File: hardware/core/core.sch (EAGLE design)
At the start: 280 parts, among them IC1 MAX481CSA, IC10 MAX481CSA, IC11 MAX481CSA, IC12 MAX481CSA, IC13 MAX481CSA, IC14 MAX481CSA, IC15 MAX481CSA, IC16 MAX481CSA, IC17 MAX481CSA, IC18 MAX481CSA, IC19 MAX481CSA, IC2 LD117AS12TR, IC20 MAX481CSA, IC21 MAX481CSA, IC3 MAX481CSA, IC4 MAX481CSA, IC5 MAX481CSA, IC6 MAX481CSA, IC7 MAX481CSA, IC8 MAX481CSA, IC9 MAX481CSA

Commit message: Nova 3.0 in progress. Needs line drivers.
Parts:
- added C35, C36: 10uf, rcl:C-USC0603
- added C6: 1uf, rcl:C-USC0805
- added D81, D86, D91: red, SparkFun-LED:LED0603
- added D82, D87, D92: green, SparkFun-LED:LED0603
- added D83, D88, D93: blue, SparkFun-LED:LED0603
- added D84, D89: white, SparkFun-LED:LED0603
- added D85, D90, D94: yellow, SparkFun-LED:LED0603
- added IC22: LD117AS12TR, v-reg:LD117AS12TR
- added R1, R107, R108, R109, R110, R111, R112, R113, R114, R115, R116, R117, R118, R119, R120, R121, R122, R123, R124, R2: 120, rcl:R-US_R0603
- added R125, R126, R127, R128, R129, R130, R139: 1k, rcl:R-US_R0603
- added R131: 2.2k, rcl:R-US_R0603
- added R132: 12k, rcl:R-US_R0603
- added R133, R134, R135, R136, R137: 10k, rcl:R-US_R0603
- added R138: 10, rcl:R-US_R1206
- added S1, S2, S3, S4, S5: MOMENTARY-SWITCH-SPST-PTH-6.0MM, SparkFun-Switches:MOMENTARY-SWITCH-SPST-PTH-6.0MM
- added ULN2: (no value), SparkFun-IC-Special-Function:ULN2803SOICW
- R68: value 68 -> 10; device rcl:R-US_R0603 -> rcl:R-US_R1206; LCSC_PART C25804 -> C17903
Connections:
- new net N$151: D84.A, R129.2
- new net N$152: D85.A, R128.2
- new net N$153: D83.A, R127.2
- new net N$154: D82.A, R126.2
- new net N$155: D81.A, R125.2
- new net N$156: D91.C, R130.1
- new net N$157: D92.C, R131.1
- new net N$158: D93.C, R132.1
- new net N$159: D94.C, R139.1
- net +12V: now also D93.A, ULN2.10
- net +3V3: now also C36.1, D86.A, D87.A, D88.A, D89.A, D90.A, D91.A, IC22.OUT, R133.1, R134.1, R135.1, R136.1, R137.1, R138.2
- net +5V: now also C35.1, C6.1, D92.A, IC22.IN, R125.1, R126.1, R127.1, R128.1, R129.1
- net 13: now also D94.A
- net 23: now also ULN2.8
- net 25: now also ULN2.7
- net 26: now also ULN2.6
- net 27: now also ULN2.5
- net 32: now also ULN2.4
- net GND: now also C35.2, C36.2, C6.2, IC22.ADJ, R130.2, R131.2, R132.2, R139.2, S1.2, S2.2, S3.2, S4.2, S5.2, ULN2.9
- net H10: now also D88.C, R135.2, S3.1
- net H11: now also D90.C, R134.2, S4.1
- net H12: now also D89.C, R133.2, S5.1
- net H13: now also ULN2.3
- net H14: now also ULN2.2
- net H15: now also ULN2.1
- net H8: now also D86.C, R137.2, S1.1
- net H9: now also D87.C, R136.2, S2.1
- net N$108: now also R1.2
- net N$109: now also R1.1
- net N$110: now also R2.2
- net N$111: now also R2.1
- net N$112: now also R107.2
- net N$113: now also R107.1
- net N$114: now also R108.2
- net N$115: now also R108.1
- net N$116: now also R109.2
- net N$117: now also R109.1
- net N$118: now also R110.2
- net N$119: now also R110.1
- net N$120: now also R111.2
- net N$121: now also R111.1
- net N$122: now also R112.2
- net N$123: now also R112.1
- net N$124: now also R113.2
- net N$125: now also R113.1
- net N$126: now also R114.2
- net N$127: now also R114.1
- net N$128: now also R115.2
- net N$129: now also R115.1
- net N$130: now also R116.2
- net N$131: now also R116.1
- net N$132: now also R117.2
- net N$133: now also R117.1
- net N$134: now also R118.2
- net N$135: now also R118.1
- net N$136: now also R119.2
- net N$137: now also R119.1
- net N$138: now also R120.2
- net N$139: now also R120.1
- net N$140: now also R121.2
- net N$141: now also R121.1
- net N$142: now also R122.2
- net N$143: now also R122.1
- net N$144: now also R123.2
- net N$145: now also R123.1
- net N$146: now also R124.2
- net N$147: now also R124.1
- net N$148: now also ULN2.16
- net N$149: now also ULN2.17
- net N$150: now also ULN2.18
- net N$51: now also D81.C, ULN2.11
- net N$56: now also D82.C, ULN2.12
- net N$57: now also D83.C, ULN2.13
- net N$58: now also D85.C, ULN2.14
- net N$59: now also D84.C, ULN2.15
- net N$89: now also R138.1
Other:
- note added: "TODO: Power light Safety Engaged Light"
- moved on the sheet: ACCESSORY, ACCESSORY_GPIO, ULN1

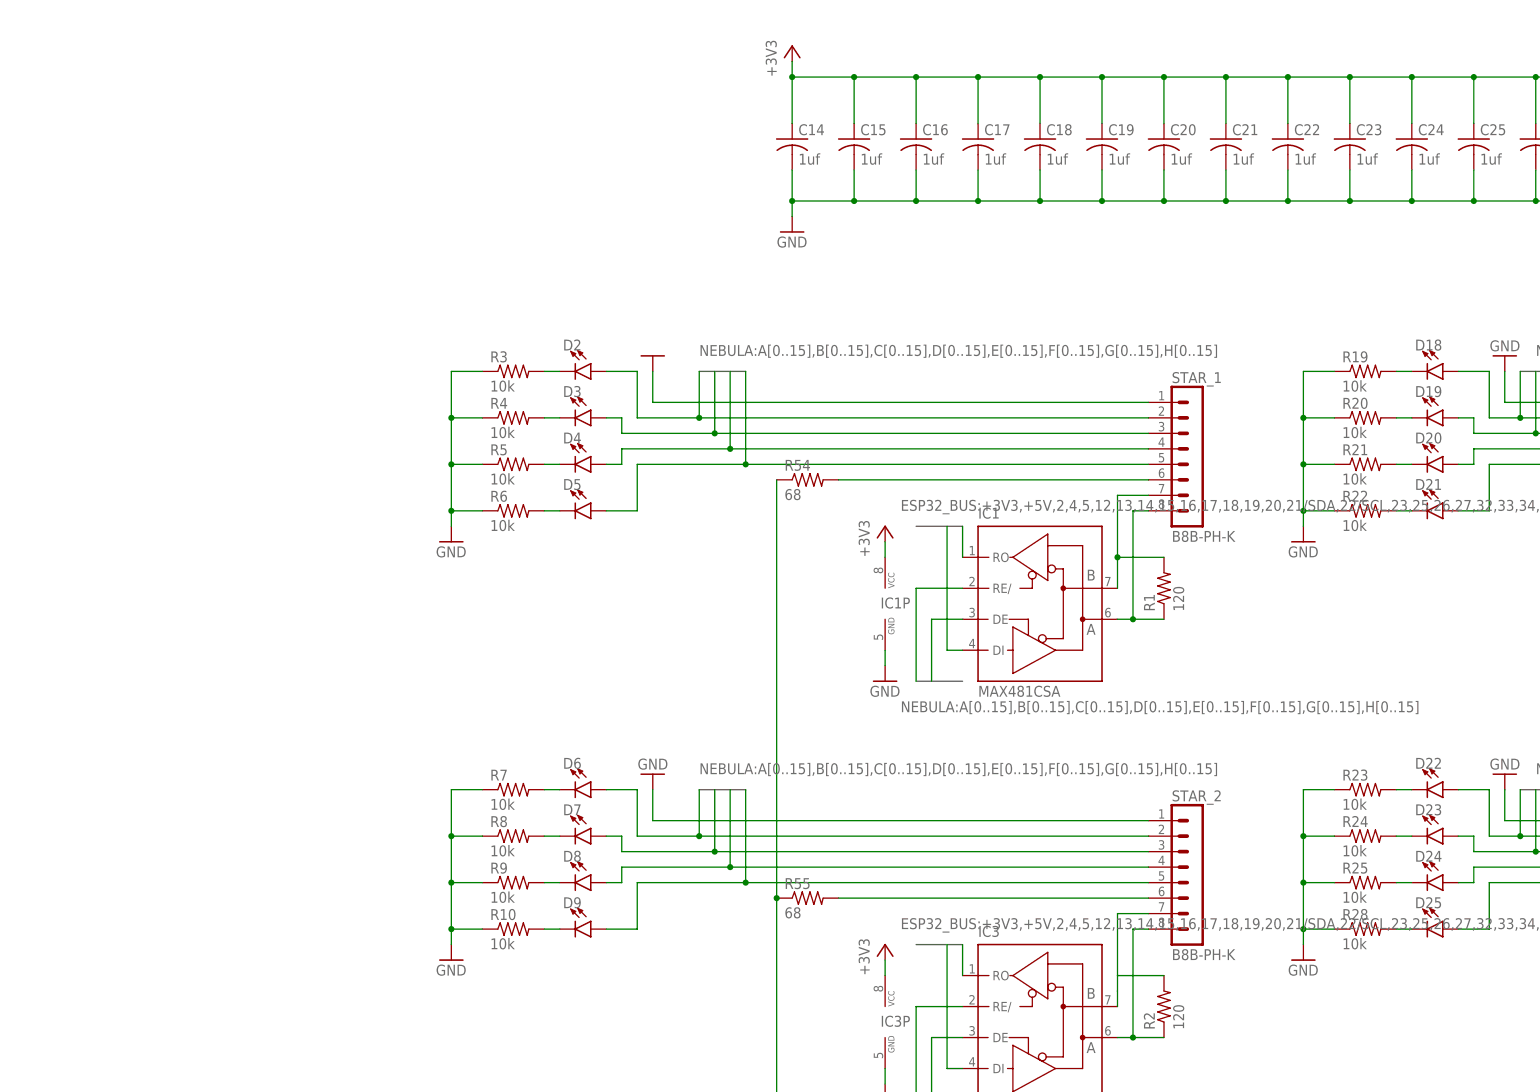
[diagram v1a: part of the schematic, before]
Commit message: start of adding ULN to the outputs
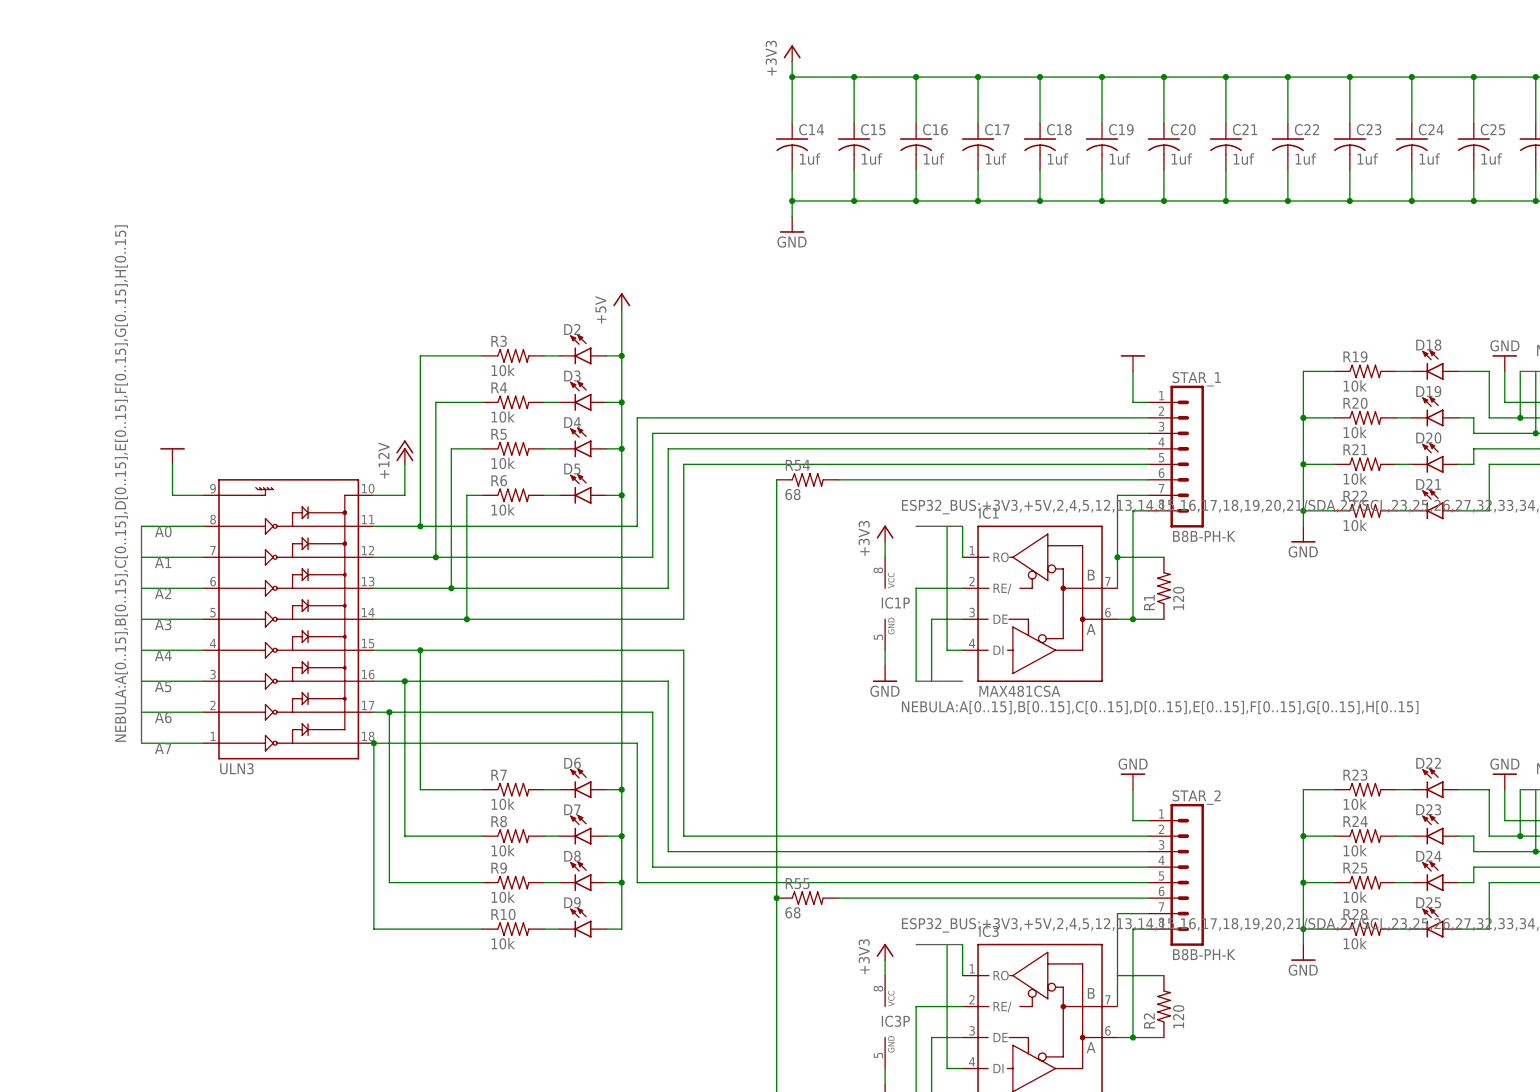
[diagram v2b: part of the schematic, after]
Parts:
- added ULN3: (no value), SparkFun-IC-Special-Function:ULN2803SOICW
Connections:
- new net N$160: R3.1, STAR_1.2, ULN3.11
- new net N$161: R4.1, STAR_1.3, ULN3.12
- new net N$162: R5.1, STAR_1.4, ULN3.13
- new net N$163: R6.1, STAR_1.5, ULN3.14
- new net N$164: R10.1, STAR_2.5, ULN3.18
- new net N$165: R9.1, STAR_2.4, ULN3.17
- new net N$166: R8.1, STAR_2.3, ULN3.16
- new net N$167: R7.1, STAR_2.2, ULN3.15
- net +12V: now also ULN3.10
- net +5V: now also D2.A, D3.A, D4.A, D5.A, D6.A, D7.A, D8.A, D9.A
- net A0: now also ULN3.8; no longer D2.A, STAR_1.2
- net A1: now also ULN3.7; no longer D3.A, STAR_1.3
- net A2: now also ULN3.6; no longer D4.A, STAR_1.4
- net A3: now also ULN3.5; no longer D5.A, STAR_1.5
- net A4: now also ULN3.4; no longer D6.A, STAR_2.2
- net A5: now also ULN3.3; no longer D7.A, STAR_2.3
- net A6: now also ULN3.2; no longer D8.A, STAR_2.4
- net A7: now also ULN3.1; no longer D9.A, STAR_2.5
- net GND: now also ULN3.9; no longer R10.1, R3.1, R4.1, R5.1, R6.1, R7.1, R8.1, R9.1
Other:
- moved on the sheet: D2, D3, D4, D5, R3, R4, R5, R6

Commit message: More Progress
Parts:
- added C37, C38, C39, C40, C41, C42, C43, C44, C45, C46, C47, C48, C49, C50, C51, C52, C53, C54, C55, C56, C57, C58, C59, C60, C61, C62, C63, C64, C65, C66, C67, C68, C73, C74, C75, C76, C77, C78, C79, C80, C81, C82, C83, C84, C85, C86, C87, C88: 1nf, rcl:C-USC0603
- added C69, C70, C71, C72, C89: 2200uf, rcl:CPOL-USE5-13
- added C90: 1uf, rcl:C-USC0805
- added C91, C92: 10uf, rcl:C-USC0603
- added IC23: LD117AS12TR, v-reg:LD117AS12TR
- added R140, R141, R142, R143, R144, R145, R146, R147, R148, R149, R150, R151, R152, R153, R154, R155, R156, R157, R158, R159, R160, R161, R162, R163, R164, R165, R166, R167, R168, R169, R170, R171, R172, R173, R174, R175, R176, R177, R178, R179, R180, R181, R182, R183, R184, R185, R186, R187, R188, R189, R190, R191, R192, R193, R194, R195, R196, R197, R198, R199, R200, R201, R202, R203, R204, R205, R206, R207, R208, R209, R210, R211, R212, R213, R214, R215, R216, R217, R218, R219: 68, rcl:R-US_R0603
- added ULN10, ULN11, ULN12, ULN4, ULN5, ULN6, ULN7, ULN8, ULN9: (no value), SparkFun-IC-Special-Function:ULN2803SOICW
- LEDARRAY: device SparkFun-Connectors:CONN_03 -> SparkFun-Connectors:CONN_03LONGPADS
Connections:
- new net N$168: R143.2, STAR_1.2
- new net N$169: R142.2, STAR_1.3
- new net N$170: R141.2, STAR_1.4
- new net N$171: R140.2, STAR_1.5
- new net N$172: R147.2, STAR_2.2
- new net N$173: R146.2, STAR_2.3
- new net N$174: R145.2, STAR_2.4
- new net N$175: R144.2, STAR_2.5
- new net N$176: R151.2, STAR_3.2
- new net N$177: R150.2, STAR_3.3
- new net N$178: R149.2, STAR_3.4
- new net N$179: R148.2, STAR_3.5
- new net N$180: R155.2, STAR_4.2
- new net N$181: R154.2, STAR_4.3
- new net N$182: R153.2, STAR_4.4
- new net N$183: R152.2, STAR_4.5
- new net N$184: C45.1, R11.1, R151.1, ULN4.11
- new net N$185: C46.1, R12.1, R150.1, ULN4.12
- new net N$186: C47.1, R13.1, R149.1, ULN4.13
- new net N$187: C48.1, R14.1, R148.1, ULN4.14
- new net N$188: C52.1, R152.1, R18.1, ULN4.18
- new net N$189: C51.1, R153.1, R17.1, ULN4.17
- new net N$190: C50.1, R154.1, R16.1, ULN4.16
- new net N$191: C49.1, R15.1, R155.1, ULN4.15
- new net N$192: C53.1, R159.1, R19.1, ULN5.11
- new net N$193: C56.1, R156.1, R22.1, ULN5.14
- new net N$194: C55.1, R157.1, R21.1, ULN5.13
- new net N$195: C54.1, R158.1, R20.1, ULN5.12
- new net N$196: C60.1, R160.1, R28.1, ULN5.18
- new net N$197: C59.1, R161.1, R25.1, ULN5.17
- new net N$198: C58.1, R162.1, R24.1, ULN5.16
- new net N$199: C57.1, R163.1, R23.1, ULN5.15
- new net N$200: R159.2, STAR_5.2
- new net N$201: R158.2, STAR_5.3
- new net N$202: R157.2, STAR_5.4
- new net N$203: R156.2, STAR_5.5
- new net N$204: R163.2, STAR_6.2
- new net N$205: R162.2, STAR_6.3
- new net N$206: R161.2, STAR_6.4
- new net N$207: R160.2, STAR_6.5
- new net N$208: R167.2, STAR_7.2
- new net N$209: R166.2, STAR_7.3
- new net N$210: R165.2, STAR_7.4
- new net N$211: R164.2, STAR_7.5
- new net N$212: R171.2, STAR_8.2
- new net N$213: R170.2, STAR_8.3
- new net N$214: R169.2, STAR_8.4
- new net N$215: R168.2, STAR_8.5
- new net N$216: C61.1, R167.1, R29.1, ULN6.11
- new net N$217: C62.1, R166.1, R30.1, ULN6.12
- new net N$218: C63.1, R165.1, R31.1, ULN6.13
- new net N$219: C64.1, R164.1, R32.1, ULN6.14
- new net N$220: C68.1, R168.1, R36.1, ULN6.18
- new net N$221: C67.1, R169.1, R35.1, ULN6.17
- new net N$222: C66.1, R170.1, R34.1, ULN6.16
- new net N$223: C65.1, R171.1, R33.1, ULN6.15
- new net N$224: R175.2, STAR_9.2
- new net N$225: R179.2, STAR_10.2
- new net N$226: R178.2, STAR_10.3
- new net N$227: R174.2, STAR_9.3
- new net N$228: R173.2, STAR_9.4
- new net N$229: R172.2, STAR_9.5
- new net N$230: R177.2, STAR_10.4
- new net N$231: R176.2, STAR_10.5
- new net N$232: R183.2, STAR_11.2
- new net N$233: R182.2, STAR_11.3
- new net N$234: R181.2, STAR_11.4
- new net N$235: R180.2, STAR_11.5
- new net N$236: R187.2, STAR_12.2
- new net N$237: R186.2, STAR_12.3
- new net N$238: R185.2, STAR_12.4
- new net N$239: R184.2, STAR_12.5
- new net N$240: C73.1, R175.1, R37.1, ULN7.11
- new net N$241: C74.1, R174.1, R38.1, ULN7.12
- new net N$242: C75.1, R173.1, R39.1, ULN7.13
- new net N$243: C76.1, R172.1, R40.1, ULN7.14
- new net N$244: R191.2, STAR_13.2
- new net N$245: C79.1, R177.1, R43.1, ULN7.17
- new net N$246: C78.1, R178.1, R42.1, ULN7.16
- new net N$247: C77.1, R179.1, R41.1, ULN7.15
- new net N$248: C81.1, R183.1, R45.1, ULN8.11
- new net N$249: C82.1, R182.1, R46.1, ULN8.12
- new net N$250: C83.1, R181.1, R47.1, ULN8.13
- new net N$251: C84.1, R180.1, R48.1, ULN8.14
- new net N$252: C80.1, R176.1, R44.1, ULN7.18
- new net N$253: C87.1, R185.1, R51.1, ULN8.17
- new net N$254: C86.1, R186.1, R50.1, ULN8.16
- new net N$255: C85.1, R187.1, R49.1, ULN8.15
- new net N$256: R190.2, STAR_13.3
- new net N$257: R189.2, STAR_13.4
- new net N$258: R188.2, STAR_13.5
- new net N$259: R196.2, STAR_14.2
- new net N$260: C88.1, R184.1, R52.1, ULN8.18
- new net N$261: R195.2, STAR_14.3
- new net N$262: R194.2, STAR_14.4
- new net N$263: R193.2, STAR_14.5
- new net N$264: R199.2, STAR_15.2
- new net N$265: R198.2, STAR_15.3
- new net N$266: R192.2, STAR_15.5
- new net N$267: R197.2, STAR_15.4
- new net N$268: R203.2, STAR_16.2
- new net N$269: R202.2, STAR_16.3
- new net N$270: R201.2, STAR_16.4
- new net N$271: R200.2, STAR_16.5
- new net N$272: R216.2, STAR_20.5
- new net N$273: R217.2, STAR_20.4
- new net N$274: R218.2, STAR_20.3
- new net N$275: R219.2, STAR_20.2
- new net N$276: R212.2, STAR_19.5
- new net N$277: R213.2, STAR_19.4
- new net N$278: R214.2, STAR_19.3
- new net N$279: R215.2, STAR_19.2
- new net N$280: R208.2, STAR_18.5
- new net N$281: R209.2, STAR_18.4
- new net N$282: R210.2, STAR_18.3
- new net N$283: R211.2, STAR_18.2
- new net N$284: R204.2, STAR_17.5
- new net N$285: R205.2, STAR_17.4
- new net N$286: R206.2, STAR_17.3
- new net N$287: R207.2, STAR_17.2
- net +12V: now also C89.+, C90.1, C92.1, IC23.IN, ULN4.10, ULN5.10, ULN6.10, ULN7.10, ULN8.10
- net +3V3: now also C70.+, C72.+
- net +5V: now also C69.+, C71.+, C91.1, D10.A, D11.A, D12.A, D13.A, D14.A, D15.A, D16.A, D17.A, D18.A, D19.A, D20.A, D21.A, D22.A, D23.A, D24.A, D25.A, D26.A, D27.A, D28.A, D29.A, D30.A, D31.A, D32.A, D33.A, D34.A, D35.A, D36.A, D37.A, D38.A, D39.A, D40.A, D41.A, D42.A, D43.A, D44.A, D45.A, D46.A, D47.A, D48.A, D49.A, IC23.OUT
- net A10: now also ULN4.6; no longer D12.A, STAR_3.4
- net A11: now also ULN4.5; no longer D13.A, STAR_3.5
- net A12: now also ULN4.4; no longer D14.A, STAR_4.2
- net A13: now also ULN4.3; no longer D15.A, STAR_4.3
- net A14: now also ULN4.2; no longer D16.A, STAR_4.4
- net A15: now also ULN4.1; no longer D17.A, STAR_4.5
- net A8: now also ULN4.8; no longer D10.A, STAR_3.2
- net A9: now also ULN4.7; no longer D11.A, STAR_3.3
- net B0: now also ULN5.8; no longer D18.A, STAR_5.2
- net B1: now also ULN5.7; no longer D19.A, STAR_5.3
- net B10: now also ULN6.6; no longer D28.A, STAR_7.4
- net B11: now also ULN6.5; no longer D29.A, STAR_7.5
- net B12: now also ULN6.4; no longer D30.A, STAR_8.2
- net B13: now also ULN6.3; no longer D31.A, STAR_8.3
- net B14: now also ULN6.2; no longer D32.A, STAR_8.4
- net B15: now also ULN6.1; no longer D33.A, STAR_8.5
- net B2: now also ULN5.6; no longer D20.A, STAR_5.4
- net B3: now also ULN5.5; no longer D21.A, STAR_5.5
- net B4: now also ULN5.4; no longer D22.A, STAR_6.2
- net B5: now also ULN5.3; no longer D23.A, STAR_6.3
- net B6: now also ULN5.2; no longer D24.A, STAR_6.4
- net B7: now also ULN5.1; no longer D25.A, STAR_6.5
- net B8: now also ULN6.8; no longer D26.A, STAR_7.2
- net B9: now also ULN6.7; no longer D27.A, STAR_7.3
- net C0: now also ULN7.8; no longer D34.A, STAR_9.2
- net C1: now also ULN7.7; no longer D35.A, STAR_9.3
- net C10: now also ULN8.6; no longer D44.A, STAR_11.4
- net C11: now also ULN8.5; no longer D45.A, STAR_11.5
- net C12: now also ULN8.4; no longer D46.A, STAR_12.2
- net C13: now also ULN8.3; no longer D47.A, STAR_12.3
- net C14: now also ULN8.2; no longer D48.A, STAR_12.4
- net C15: now also ULN8.1; no longer D49.A, STAR_12.5
- net C2: now also ULN7.6; no longer D36.A, STAR_9.4
- net C3: now also ULN7.5; no longer D37.A, STAR_9.5
- net C4: now also ULN7.4; no longer D38.A, STAR_10.2
- net C5: now also ULN7.3; no longer D39.A, STAR_10.3
- net C6: now also ULN7.2; no longer D40.A, STAR_10.4
- net C7: now also ULN7.1; no longer D41.A, STAR_10.5
- net C8: now also ULN8.8; no longer D42.A, STAR_11.2
- net C9: now also ULN8.7; no longer D43.A, STAR_11.3
- net D0: no longer D1.A, STAR_13.2
- net D1: no longer D50.A, STAR_13.3
- net D10: no longer D59.A, STAR_15.4
- net D11: no longer D60.A, STAR_15.5
- net D12: no longer D61.A, STAR_16.2
- net D13: no longer D62.A, STAR_16.3
- net D14: no longer D63.A, STAR_16.4
- net D15: no longer D64.A, STAR_16.5
- net D2: no longer D51.A, STAR_13.4
- net D3: no longer D52.A, STAR_13.5
- net D4: no longer D53.A, STAR_14.2
- net D5: no longer D54.A, STAR_14.3
- net D6: no longer D55.A, STAR_14.4
- net D7: no longer D56.A, STAR_14.5
- net D8: no longer D57.A, STAR_15.2
- net D9: no longer D58.A, STAR_15.3
- net E0: no longer D65.A, STAR_17.2
- net E1: no longer D66.A, STAR_17.3
- net E10: no longer D75.A, STAR_19.4
- net E11: no longer D76.A, STAR_19.5
- net E12: no longer D77.A, STAR_20.2
- net E13: no longer D78.A, STAR_20.3
- net E14: no longer D79.A, STAR_20.4
- net E15: no longer D80.A, STAR_20.5
- net E2: no longer D67.A, STAR_17.4
- net E3: no longer D68.A, STAR_17.5
- net E4: no longer D69.A, STAR_18.2
- net E5: no longer D70.A, STAR_18.3
- net E6: no longer D71.A, STAR_18.4
- net E7: no longer D72.A, STAR_18.5
- net E8: no longer D73.A, STAR_19.2
- net E9: no longer D74.A, STAR_19.3
- net GND: now also C37.2, C38.2, C39.2, C40.2, C41.2, C42.2, C43.2, C44.2, C45.2, C46.2, C47.2, C48.2, C49.2, C50.2, C51.2, C52.2, C53.2, C54.2, C55.2, C56.2, C57.2, C58.2, C59.2, C60.2, C61.2, C62.2, C63.2, C64.2, C65.2, C66.2, C67.2, C68.2, C69.-, C70.-, C71.-, C72.-, C73.2, C74.2, C75.2, C76.2, C77.2, C78.2, C79.2, C80.2, C81.2, C82.2, C83.2, C84.2, C85.2, C86.2, C87.2, C88.2, C89.-, C90.2, C91.2, C92.2, IC23.ADJ, ULN4.9, ULN5.9, ULN6.9, ULN7.9, ULN8.9; no longer R11.1, R12.1, R13.1, R14.1, R15.1, R16.1, R17.1, R18.1, R19.1, R20.1, R21.1, R22.1, R23.1, R24.1, R25.1, R28.1, R29.1, R30.1, R31.1, R32.1, R33.1, R34.1, R35.1, R36.1, R37.1, R38.1, R39.1, R40.1, R41.1, R42.1, R43.1, R44.1, R45.1, R46.1, R47.1, R48.1, R49.1, R50.1, R51.1, R52.1
- net N$160: now also C37.1, R143.1; no longer STAR_1.2
- net N$161: now also C38.1, R142.1; no longer STAR_1.3
- net N$162: now also C39.1, R141.1; no longer STAR_1.4
- net N$163: now also C40.1, R140.1; no longer STAR_1.5
- net N$164: now also C44.1, R144.1; no longer STAR_2.5
- net N$165: now also C43.1, R145.1; no longer STAR_2.4
- net N$166: now also C42.1, R146.1; no longer STAR_2.3
- net N$167: now also C41.1, R147.1; no longer STAR_2.2
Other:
- moved on the sheet: C10, C11, C12, C13, C14, C15, C16, C17, C18, C19, C20, C21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

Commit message: Schematic Capture is complete
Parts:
- added C100, C101, C102, C103, C104, C105, C106, C107, C108, C109, C110, C111, C112, C113, C114, C115, C116, C117, C118, C119, C120, C121, C122, C123, C124, C93, C94, C95, C96, C97, C98, C99: 1nf, rcl:C-USC0603
- added JP2, JP3: (no value), pinhead:PINHD-1X4
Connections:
- new net N$288: C97.1, R199.1, R75.1, ULN10.11
- new net N$289: C98.1, R198.1, R76.1, ULN10.12
- new net N$290: C99.1, R197.1, R77.1, ULN10.13
- new net N$291: C100.1, R192.1, R78.1, ULN10.14
- new net N$292: C108.1, R200.1, R82.1, ULN10.18
- new net N$293: C107.1, R201.1, R81.1, ULN10.17
- new net N$294: C106.1, R202.1, R80.1, ULN10.16
- new net N$295: C105.1, R203.1, R79.1, ULN10.15
- new net N$296: C93.1, R191.1, R53.1, ULN9.11
- new net N$297: C94.1, R190.1, R66.1, ULN9.12
- new net N$298: C95.1, R189.1, R69.1, ULN9.13
- new net N$299: C96.1, R188.1, R70.1, ULN9.14
- new net N$300: C104.1, R193.1, R74.1, ULN9.18
- new net N$301: C103.1, R194.1, R73.1, ULN9.17
- new net N$302: C102.1, R195.1, R72.1, ULN9.16
- new net N$303: C101.1, R196.1, R71.1, ULN9.15
- new net N$304: C109.1, R207.1, R87.1, ULN11.11
- new net N$305: C110.1, R206.1, R88.1, ULN11.12
- new net N$306: C111.1, R205.1, R89.1, ULN11.13
- new net N$307: C112.1, R204.1, R90.1, ULN11.14
- new net N$308: C116.1, R208.1, R94.1, ULN11.18
- new net N$309: C115.1, R209.1, R93.1, ULN11.17
- new net N$310: C114.1, R210.1, R92.1, ULN11.16
- new net N$311: C113.1, R211.1, R91.1, ULN11.15
- new net N$312: C117.1, R215.1, R95.1, ULN12.11
- new net N$313: C118.1, R214.1, R96.1, ULN12.12
- new net N$314: C119.1, R213.1, R97.1, ULN12.13
- new net N$315: C120.1, R212.1, R98.1, ULN12.14
- new net N$316: C124.1, R102.1, R216.1, ULN12.18
- new net N$317: C123.1, R101.1, R217.1, ULN12.17
- new net N$318: C122.1, R100.1, R218.1, ULN12.16
- new net N$319: C121.1, R219.1, R99.1, ULN12.15
- net +12V: now also ULN10.10, ULN11.10, ULN12.10, ULN9.10
- net +3V3: now also JP2.4, JP3.1
- net +5V: now also D1.A, D50.A, D51.A, D52.A, D53.A, D54.A, D55.A, D56.A, D57.A, D58.A, D59.A, D60.A, D61.A, D62.A, D63.A, D64.A, D65.A, D66.A, D67.A, D68.A, D69.A, D70.A, D71.A, D72.A, D73.A, D74.A, D75.A, D76.A, D77.A, D78.A, D79.A, D80.A
- net 2: now also JP2.2
- net 21/SDA: now also JP3.4
- net 22/SCL: now also JP3.3
- net 5: now also JP2.3
- net D0: now also ULN9.8
- net D1: now also ULN9.7
- net D10: now also ULN10.6
- net D11: now also ULN10.5
- net D12: now also ULN10.4
- net D13: now also ULN10.3
- net D14: now also ULN10.2
- net D15: now also ULN10.1
- net D2: now also ULN9.6
- net D3: now also ULN9.5
- net D4: now also ULN9.4
- net D5: now also ULN9.3
- net D6: now also ULN9.2
- net D7: now also ULN9.1
- net D8: now also ULN10.8
- net D9: now also ULN10.7
- net E0: now also ULN11.8
- net E1: now also ULN11.7
- net E10: now also ULN12.6
- net E11: now also ULN12.5
- net E12: now also ULN12.4
- net E13: now also ULN12.3
- net E14: now also ULN12.2
- net E15: now also ULN12.1
- net E2: now also ULN11.6
- net E3: now also ULN11.5
- net E4: now also ULN11.4
- net E5: now also ULN11.3
- net E6: now also ULN11.2
- net E7: now also ULN11.1
- net E8: now also ULN12.8
- net E9: now also ULN12.7
- net GND: now also C100.2, C101.2, C102.2, C103.2, C104.2, C105.2, C106.2, C107.2, C108.2, C109.2, C110.2, C111.2, C112.2, C113.2, C114.2, C115.2, C116.2, C117.2, C118.2, C119.2, C120.2, C121.2, C122.2, C123.2, C124.2, C93.2, C94.2, C95.2, C96.2, C97.2, C98.2, C99.2, JP2.1, JP3.2, ULN10.9, ULN11.9, ULN12.9, ULN9.9; no longer R100.1, R101.1, R102.1, R53.1, R66.1, R69.1, R70.1, R71.1, R72.1, R73.1, R74.1, R75.1, R76.1, R77.1, R78.1, R79.1, R80.1, R81.1, R82.1, R87.1, R88.1, R89.1, R90.1, R91.1, R92.1, R93.1, R94.1, R95.1, R96.1, R97.1, R98.1, R99.1
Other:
- moved on the sheet: D53, D54, D55, D56, D61, D62, D63, D64, D65, D66, D67, D68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

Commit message: Completed v3
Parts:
- removed ULN1: (no value), SparkFun-IC-Special-Function:ULN2803SOIC
- added I2C_1: (no value), pinhead:PINHD-1X4
- renumbered JP3 to I2C_2
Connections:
- net +12V: no longer ULN1.10
- net +3V3: now also I2C_1.1
- net 21/SDA: now also I2C_1.4
- net 22/SCL: now also I2C_1.3
- net 23: no longer ULN1.8
- net 25: no longer ULN1.7
- net 26: no longer ULN1.6
- net 27: no longer ULN1.5
- net 32: no longer ULN1.4
- net GND: now also I2C_1.2; no longer ULN1.9
- net H13: no longer ULN1.3
- net H14: no longer ULN1.2
- net H15: no longer ULN1.1
- net N$148: no longer ULN1.16
- net N$149: no longer ULN1.17
- net N$150: no longer ULN1.18
- net N$51: no longer ULN1.11
- net N$56: no longer ULN1.12
- net N$57: no longer ULN1.13
- net N$58: no longer ULN1.14
- net N$59: no longer ULN1.15
